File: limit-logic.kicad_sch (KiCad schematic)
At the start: 6 parts, among them U17001 CD4044, U17002 CD4044, U17003 CD4078

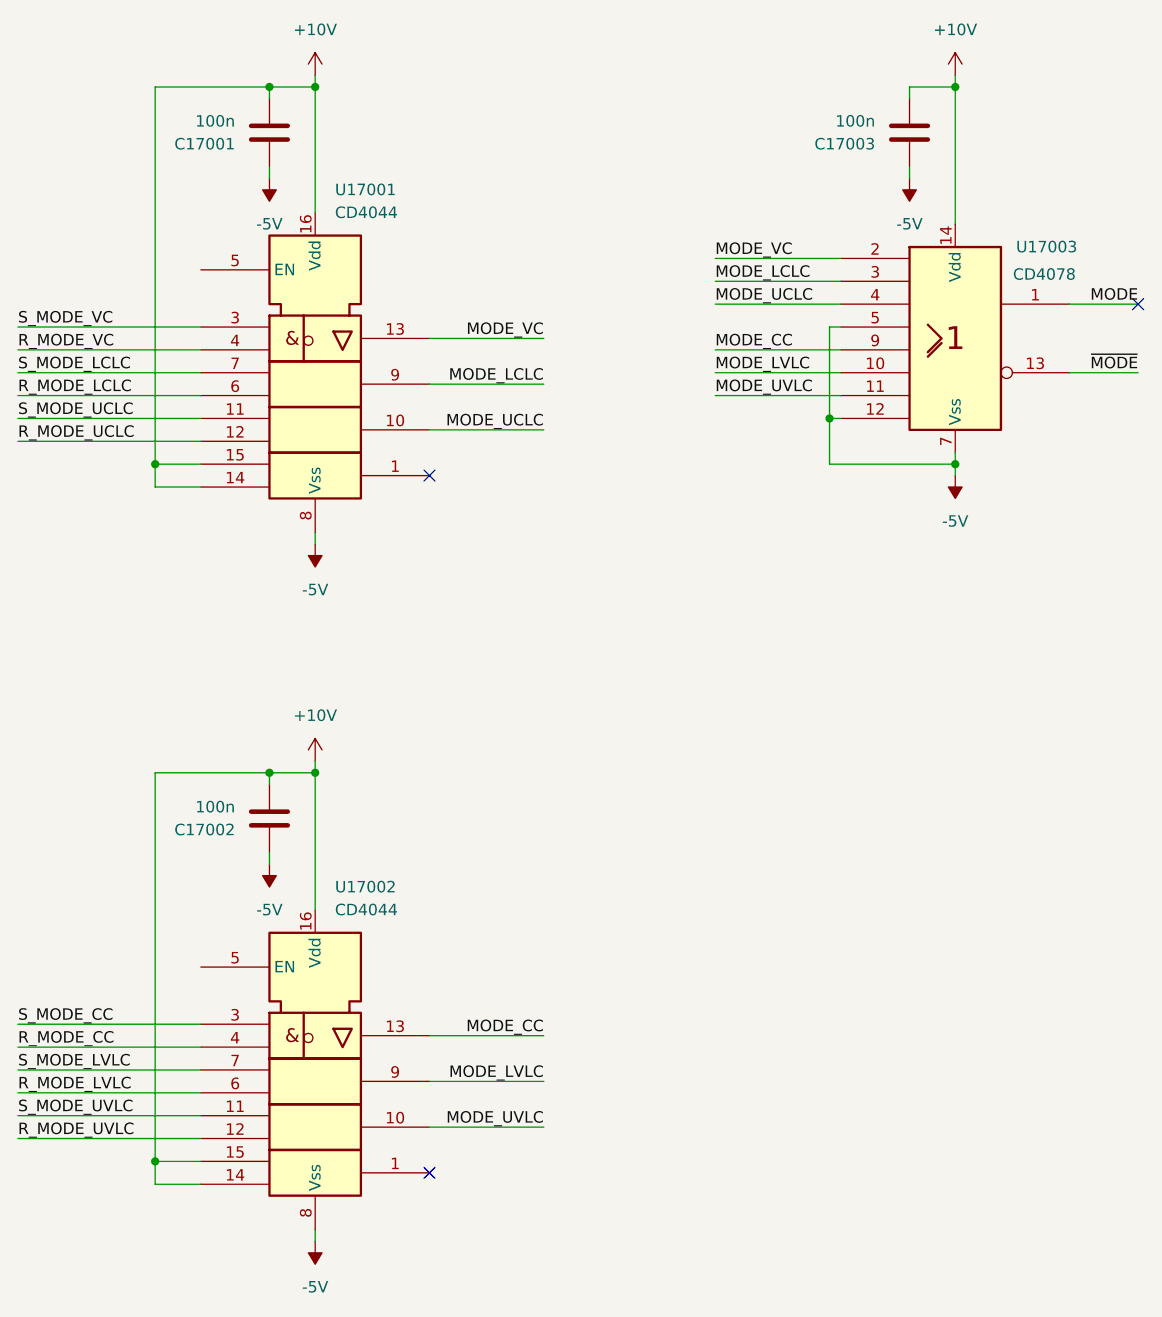
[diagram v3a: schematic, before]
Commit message: fix limit-logic SR latch positiv logic 4043
4043 is positive logic, not wrongly used 4044
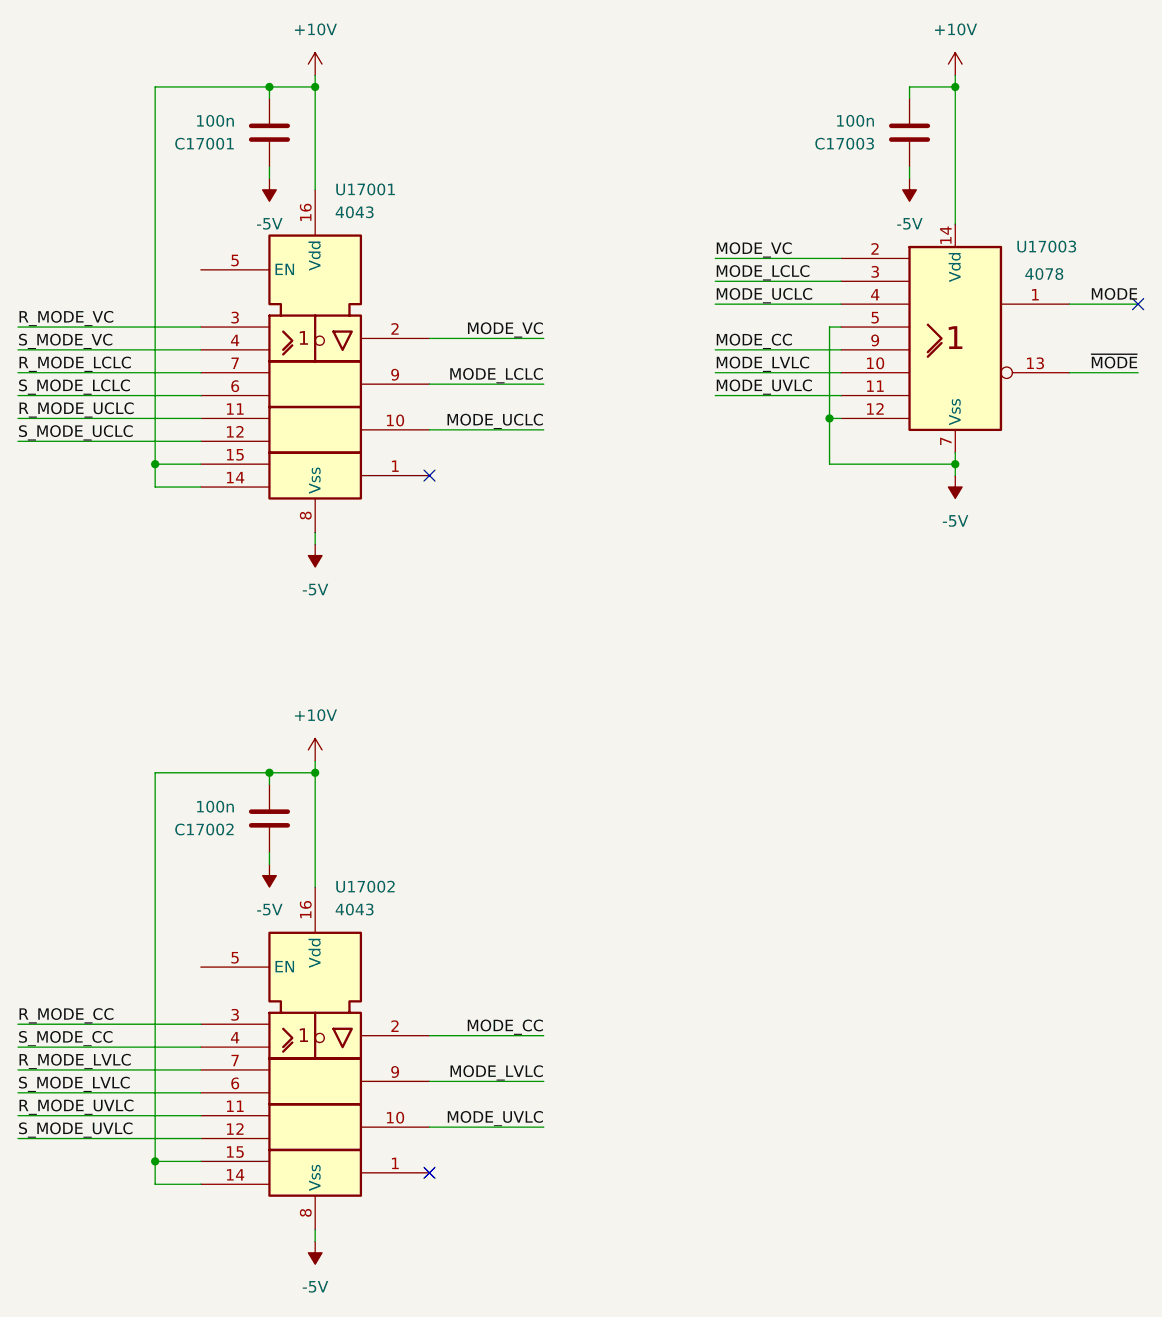
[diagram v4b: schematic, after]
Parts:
- removed U17002: CD4044, Package_SO:SOIC-16_3.9x9.9mm_P1.27mm, symbol pss:4044
- added U17002: 4043, Package_SO:SOIC-16_3.9x9.9mm_P1.27mm, symbol pss:4043
- U17001: value CD4044 -> 4043; symbol pss:4044 -> pss:4043; MPN CD4044BDR -> CD4043BDR; VPN 595-CD4044BDR -> 595-CD4043BDR
- U17003: value CD4078 -> 4078
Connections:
- net +10V: now also U17002.14, U17002.15, U17002.16 (Vdd)
- net -5V: now also U17002.8 (Vss)
- net MODE_CC: now also U17002.2
- net MODE_LVLC: now also U17002.9
- net MODE_UVLC: now also U17002.10
- net MODE_VC: now also U17001.2; no longer U17001.13
- net R_MODE_CC: now also U17002.3
- net R_MODE_LCLC: now also U17001.7; no longer U17001.6
- net R_MODE_LVLC: now also U17002.7
- net R_MODE_UCLC: now also U17001.11; no longer U17001.12
- net R_MODE_UVLC: now also U17002.11
- net R_MODE_VC: now also U17001.3; no longer U17001.4
- net S_MODE_CC: now also U17002.4
- net S_MODE_LCLC: now also U17001.6; no longer U17001.7
- net S_MODE_LVLC: now also U17002.6
- net S_MODE_UCLC: now also U17001.12; no longer U17001.11
- net S_MODE_UVLC: now also U17002.12
- net S_MODE_VC: now also U17001.4; no longer U17001.3
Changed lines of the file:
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@@
+	(wire
+		(pts
+			(xy 177.8 102.87) (xy 177.8 115.57)
+		)
+		(stroke
+			(width 0)
+			(type default)
+		)
+	)
 	(wire
 		(pts
@@
 	(wire
 		(pts
-			(xy 177.8 102.87) (xy 177.8 118.11)
-		)
-		(stroke
-			(width 0)
-			(type default)
-		)
-	)
-	(wire
-		(pts
 			(xy 177.8 25.4) (xy 177.8 26.67)
 		)
@@
 	(wire
 		(pts
-			(xy 177.8 26.67) (xy 177.8 40.64)
+			(xy 177.8 26.67) (xy 177.8 38.1)
 		)
 		(stroke
@@
 	)
 	(label "R_MODE_CC"
-		(at 144.78 133.35 0)
+		(at 144.78 130.81 0)
 		(fields_autoplaced yes)
 		(effects
@@
 	)
 	(label "R_MODE_LCLC"
-		(at 144.78 60.96 0)
+		(at 144.78 58.42 0)
 		(fields_autoplaced yes)
 		(effects
@@
 	)
 	(label "S_MODE_UCLC"
+		(at 144.78 66.04 0)
+		(fields_autoplaced yes)
+		(effects
+			(font
+				(size 1.27 1.27)
+			)
+			(justify left bottom)
+		)
+	)
+	(label "R_MODE_VC"
+		(at 144.78 53.34 0)
+		(fields_autoplaced yes)
+		(effects
+			(font
+				(size 1.27 1.27)
+			)
+			(justify left bottom)
+		)
+	)
+	(label "R_MODE_UCLC"
 		(at 144.78 63.5 0)
 		(fields_autoplaced yes)
@@
 		)
 	)
-	(label "R_MODE_VC"
-		(at 144.78 55.88 0)
-		(fields_autoplaced yes)
-		(effects
-			(font
-				(size 1.27 1.27)
-			)
-			(justify left bottom)
-		)
-	)
-	(label "R_MODE_UCLC"
-		(at 144.78 66.04 0)
-		(fields_autoplaced yes)
-		(effects
-			(font
-				(size 1.27 1.27)
-			)
-			(justify left bottom)
-		)
-	)
 	(label "S_MODE_LVLC"
-		(at 144.78 135.89 0)
+		(at 144.78 138.43 0)
 		(fields_autoplaced yes)
 		(effects
@@
 	)
 	(label "S_MODE_LCLC"
-		(at 144.78 58.42 0)
+		(at 144.78 60.96 0)
 		(fields_autoplaced yes)
 		(effects
@@
 	)
 	(label "R_MODE_LVLC"
-		(at 144.78 138.43 0)
+		(at 144.78 135.89 0)
 		(fields_autoplaced yes)
 		(effects
@@
 	)
 	(label "S_MODE_VC"
-		(at 144.78 53.34 0)
+		(at 144.78 55.88 0)
 		(fields_autoplaced yes)
 		(effects
@@
 	)
 	(label "S_MODE_CC"
-		(at 144.78 130.81 0)
+		(at 144.78 133.35 0)
 		(fields_autoplaced yes)
 		(effects
@@
 	)
 	(label "S_MODE_UVLC"
+		(at 144.78 143.51 0)
+		(fields_autoplaced yes)
+		(effects
+			(font
+				(size 1.27 1.27)
+			)
+			(justify left bottom)
+		)
+	)
+	(label "R_MODE_UVLC"
 		(at 144.78 140.97 0)
-		(fields_autoplaced yes)
-		(effects
-			(font
-				(size 1.27 1.27)
-			)
-			(justify left bottom)
-		)
-	)
-	(label "R_MODE_UVLC"
-		(at 144.78 143.51 0)
 		(fields_autoplaced yes)
 		(effects
@@
 	)
 	(symbol
+		(lib_id "pss:4043")
+		(at 177.8 130.81 0)
+		(unit 1)
+		(exclude_from_sim no)
+		(in_bom yes)
+		(on_board yes)
+		(dnp no)
+		(fields_autoplaced yes)
+		(property "Reference" "U17002"
+			(at 179.9941 115.57 0)
+			(effects
+				(font
+					(size 1.27 1.27)
+				)
+				(justify left)
+			)
+		)
+		(property "Value" "4043"
+			(at 179.9941 118.11 0)
+			(effects
+				(font
+					(size 1.27 1.27)
+				)
+				(justify left)
+			)
+		)
+		(property "Footprint" "Package_SO:SOIC-16_3.9x9.9mm_P1.27mm"
+			(at 177.8 130.81 0)
+			(effects
+				(font
+					(size 1.27 1.27)
+				)
+				(hide yes)
+			)
+		)
+		(property "Datasheet" "https://www.ti.com/lit/ds/symlink/cd4043b.pdf"
+			(at 177.8 130.81 0)
+			(effects
+				(font
+					(size 1.27 1.27)
+				)
+				(hide yes)
+			)
+		)
+		(property "Description" ""
+			(at 177.8 130.81 0)
+			(effects
+				(font
+					(size 1.27 1.27)
+				)
+				(hide yes)
+			)
+		)
+		(property "MPN" "CD4043BDR"
+			(at 177.8 130.81 0)
+			(effects
+				(font
+					(size 1.27 1.27)
+				)
+				(hide yes)
+			)
+		)
+		(property "VPN" "595-CD4043BDR"
+			(at 177.8 130.81 0)
+			(effects
+				(font
+					(size 1.27 1.27)
+				)
+				(hide yes)
+			)
+		)
+		(pin "9"
+		)
+		(pin "5"
+		)
+		(pin "4"
+		)
+		(pin "2"
+		)
+		(pin "8"
+		)
+		(pin "6"
+		)
+		(pin "3"
+		)
+		(pin "16"
+		)
+		(pin "15"
+		)
+		(pin "12"
+		)
+		(pin "1"
+		)
+		(pin "14"
+		)
+		(pin "10"
+		)
+		(pin "11"
+		)
+		(pin "7"
+		)
+		(instances
+			(project "pss"
+				(path "/3c438cf7-9350-4e9f-8115-1deba8984176/663aa7df-ca78-4d48-8732-ebacb327e46a"
+					(reference "U17002")
+					(unit 1)
+				)
+			)
+		)
+	)
+	(symbol
 		(lib_id "pss:4078")
 		(at 248.92 54.61 0)
@@
 			)
 		)
-		(property "Value" "CD4078"
+		(property "Value" "4078"
 			(at 258.826 47.498 0)
 			(effects
@@
 				(path "/3c438cf7-9350-4e9f-8115-1deba8984176/663aa7df-ca78-4d48-8732-ebacb327e46a"
 					(reference "#PWR017007")
-					(unit 1)
-				)
-			)
-		)
-	)
-	(symbol
-		(lib_id "pss:4044")
-		(at 177.8 130.81 0)
-		(unit 1)
-		(exclude_from_sim no)
-		(in_bom yes)
-		(on_board yes)
-		(dnp no)
-		(fields_autoplaced yes)
-		(property "Reference" "U17002"
-			(at 179.9941 115.57 0)
-			(effects
-				(font
-					(size 1.27 1.27)
-				)
-				(justify left)
-			)
-		)
-		(property "Value" "CD4044"
-			(at 179.9941 118.11 0)
-			(effects
-				(font
-					(size 1.27 1.27)
-				)
-				(justify left)
-			)
-		)
-		(property "Footprint" "Package_SO:SOIC-16_3.9x9.9mm_P1.27mm"
-			(at 177.8 130.81 0)
-			(effects
-				(font
-					(size 1.27 1.27)
-				)
-				(hide yes)
-			)
-		)
-		(property "Datasheet" "https://www.ti.com/lit/ds/symlink/cd4044b.pdf"
-			(at 177.8 130.81 0)
-			(effects
-				(font
-					(size 1.27 1.27)
-				)
-				(hide yes)
-			)
-		)
-		(property "Description" ""
-			(at 177.8 130.81 0)
-			(effects
-				(font
-					(size 1.27 1.27)
-				)
-				(hide yes)
-			)
-		)
-		(property "MPN" "CD4044BDR"
-			(at 177.8 130.81 0)
-			(effects
-				(font
-					(size 1.27 1.27)
-				)
-				(hide yes)
-			)
-		)
-		(property "VPN" "595-CD4044BDR"
-			(at 177.8 130.81 0)
-			(effects
-				(font
-					(size 1.27 1.27)
-				)
-				(hide yes)
-			)
-		)
-		(pin "9"
-		)
-		(pin "5"
-		)
-		(pin "4"
-		)
-		(pin "13"
-		)
-		(pin "8"
-		)
-		(pin "6"
-		)
-		(pin "3"
-		)
-		(pin "16"
-		)
-		(pin "15"
-		)
-		(pin "12"
-		)
-		(pin "1"
-		)
-		(pin "14"
-		)
-		(pin "10"
-		)
-		(pin "11"
-		)
-		(pin "7"
-		)
-		(instances
-			(project "pss"
-				(path "/3c438cf7-9350-4e9f-8115-1deba8984176/663aa7df-ca78-4d48-8732-ebacb327e46a"
-					(reference "U17002")
 					(unit 1)
 				)
@@
 	)
 	(symbol
-		(lib_id "pss:4044")
+		(lib_id "pss:4043")
 		(at 177.8 53.34 0)
 		(unit 1)
@@
 			)
 		)
-		(property "Value" "CD4044"
+		(property "Value" "4043"
 			(at 179.9941 40.64 0)
 			(effects
@@
 			)
 		)
-		(property "Datasheet" "https://www.ti.com/lit/ds/symlink/cd4044b.pdf"
+		(property "Datasheet" "https://www.ti.com/lit/ds/symlink/cd4043b.pdf"
 			(at 177.8 53.34 0)
 			(effects
@@
 			)
 		)
-		(property "MPN" "CD4044BDR"
+		(property "MPN" "CD4043BDR"
 			(at 177.8 53.34 0)
 			(effects
@@
 			)
 		)
-		(property "VPN" "595-CD4044BDR"
+		(property "VPN" "595-CD4043BDR"
 			(at 177.8 53.34 0)
 			(effects
@@
 		(pin "4"
 		)
-		(pin "13"
+		(pin "2"
 		)
 		(pin "8"
